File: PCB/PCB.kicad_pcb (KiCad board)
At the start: 2 copper layers, 150 x 150 mm, 14 parts

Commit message: resized and gerber
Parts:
- moved MotorFL1 58.0 mm to (99.1, 107.2), turned to 0 degrees
- moved MotorFR1 43.9 mm to (179.8, 106.6), turned to 180 degrees
- moved MotorBL1 34.5 mm to (99.1, 126.6), turned to 0 degrees
- moved MotorBR1 18.1 mm to (179.8, 126.0), turned to 180 degrees
- moved Battery1 14.7 mm to (154.8, 90.8)
- moved Buck_IN-1 9.28 mm to (163.3, 102.8)
- moved Buck_OUT-1 9.28 mm to (163.3, 122.8)
- moved Buck_IN+1 9.28 mm to (152.8, 102.8)
- moved Buck_OUT+1 9.28 mm to (152.8, 122.8)
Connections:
- PicoL1 pad 18: GND -> GND18
- PicoL1 pad 3: GND -> GND3
- PicoL1 pad 8: GND -> unconnected-(PicoL1-Pin_8-Pad8)
- PicoR1 pad 13: GND -> unconnected-(PicoR1-Pin_13-Pad13)
- PicoR1 pad 18: GND -> unconnected-(PicoR1-Pin_18-Pad18)
- PicoR1 pad 3: GND -> unconnected-(PicoR1-Pin_3-Pad3)
- PicoR1 pad 8: GND -> unconnected-(PicoR1-Pin_8-Pad8)
- QTR-8RC1 pad 11: GND -> GND3
- TB6612FNGL1 pad 1: GND -> unconnected-(TB6612FNGL1-Pin_1-Pad1)
- TB6612FNGR1 pad 3: GND -> GND18
- TB6612FNGR1 pad 8: GND -> unconnected-(TB6612FNGR1-Pin_8-Pad8)
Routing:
- net GND: track 451.5 -> 188.4 mm
- net Net-(MotorBL1-Pin_2): track 132.2 -> 45.3 mm
- net Net-(MotorBL1-Pin_1): track 138.7 -> 54.5 mm
- net Net-(MotorBR1-Pin_2): track 141.0 -> 69.4 mm
- net Net-(MotorBR1-Pin_1): track 143.3 -> 78.9 mm
- net GND18: track 0.00 -> 47.8 mm
- net GND3: track 0.00 -> 28.3 mm
- net VCC: track 77.0 -> 58.6 mm
- net /BuckOut: track 70.2 -> 63.4 mm
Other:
- board size 150 x 150 mm -> 100 x 115.5 mm

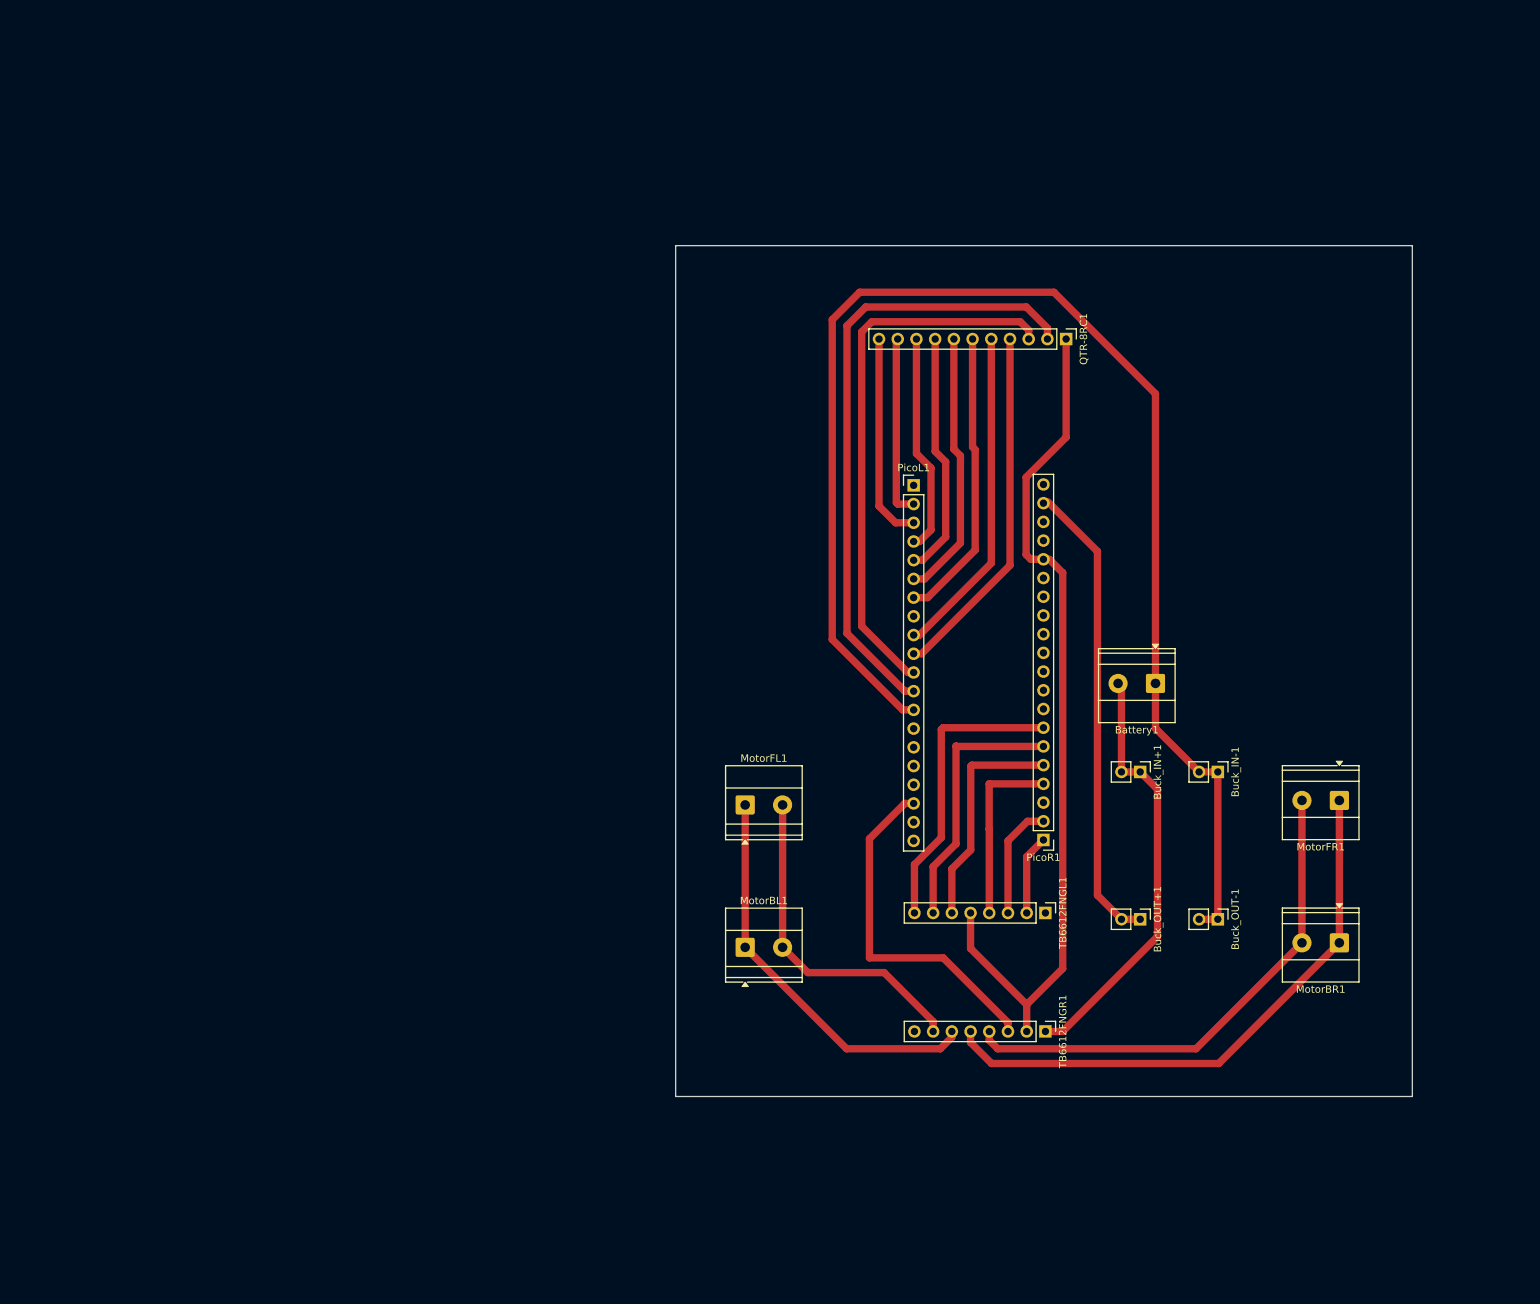
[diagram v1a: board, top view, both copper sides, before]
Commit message: page setup and pdf generation
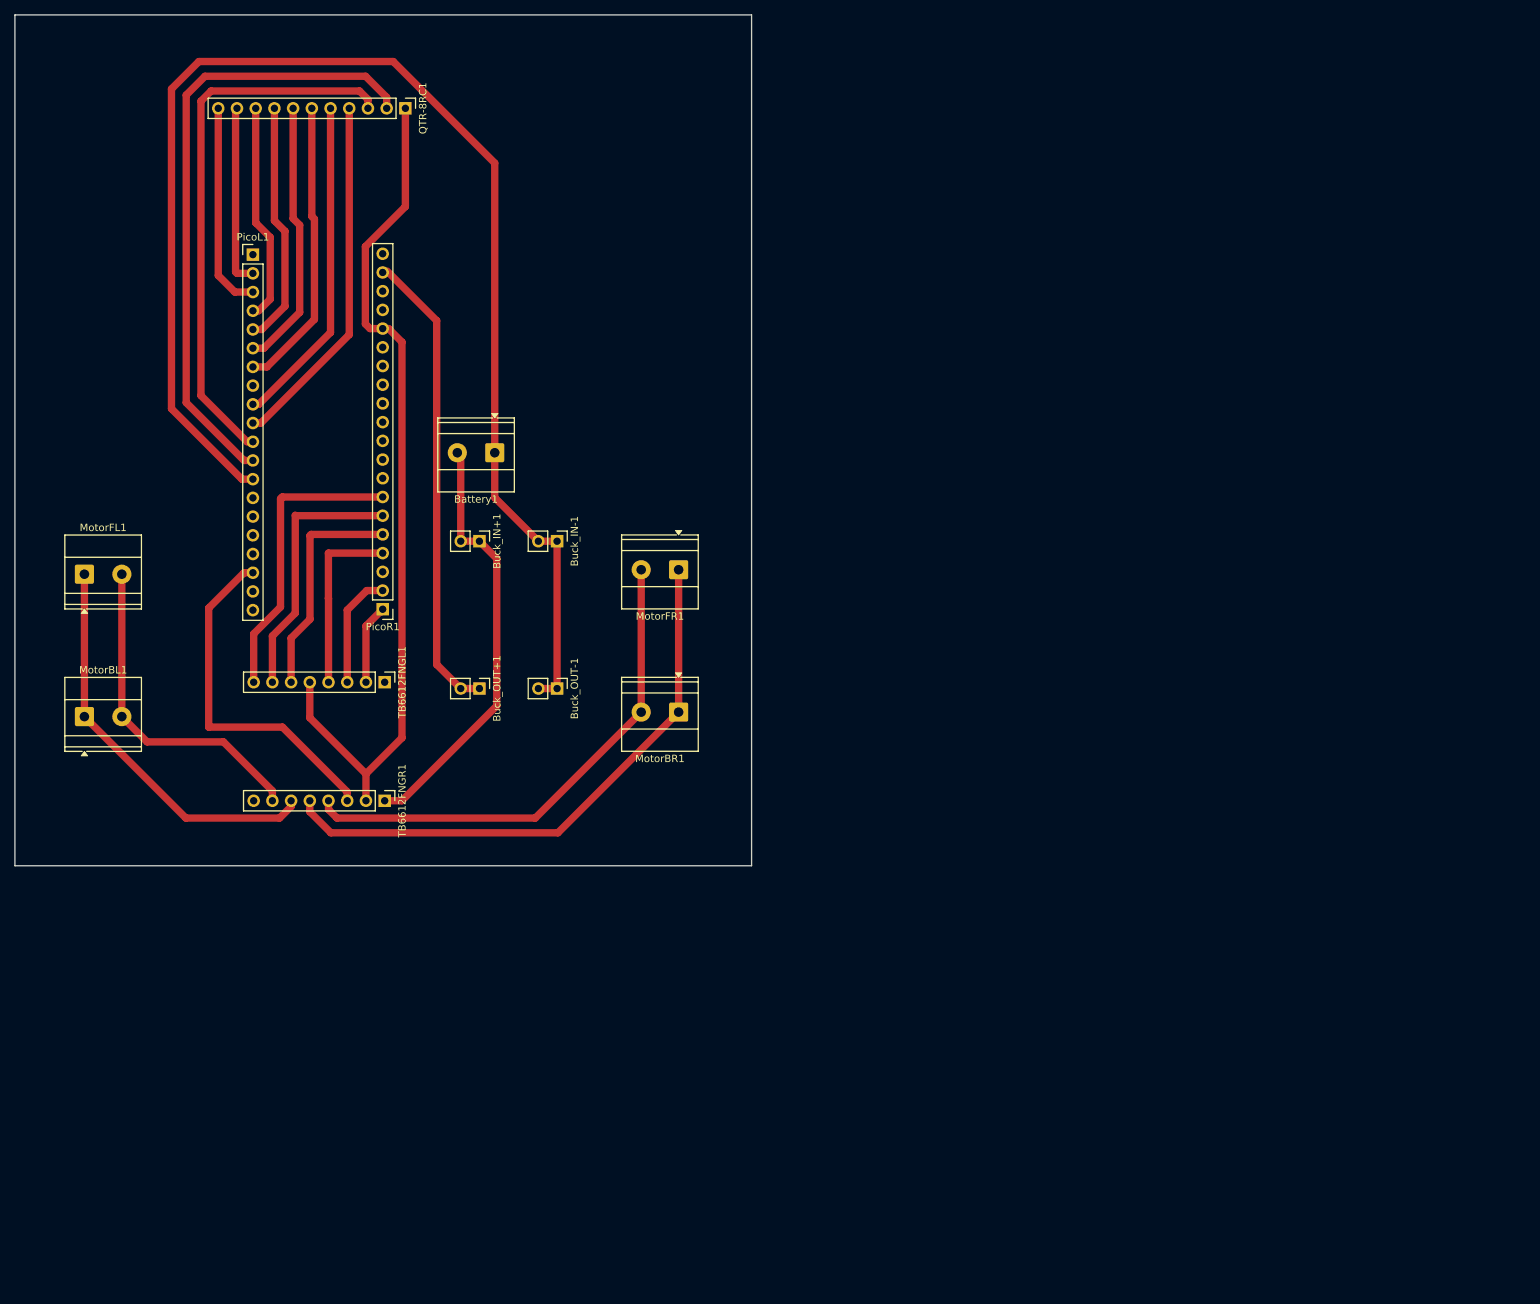
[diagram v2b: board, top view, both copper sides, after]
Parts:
- moved Battery1 95.0 mm to (65.1, 59.4)
- moved PicoR1 95.0 mm to (49.9, 80.7)
- moved Buck_IN+1 95.0 mm to (63.1, 71.4)
- moved Buck_IN-1 95.0 mm to (73.6, 71.4)
- moved Buck_OUT+1 95.0 mm to (63.1, 91.4)
- moved Buck_OUT-1 95.0 mm to (73.6, 91.4)
- moved MotorBL1 95.0 mm to (9.44, 95.3)
- moved MotorBR1 95.0 mm to (90.1, 94.6)
- moved MotorFL1 95.0 mm to (9.44, 75.9)
- moved MotorFR1 95.0 mm to (90.1, 75.3)
- moved PicoL1 95.0 mm to (32.3, 32.5)
- moved QTR-8RC1 95.0 mm to (53.0, 12.7)
- moved TB6612FNGL1 95.0 mm to (50.2, 90.6)
- moved TB6612FNGR1 95.0 mm to (50.2, 106.7)

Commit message: centralized
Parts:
- moved TB6612FNGL1 14.0 mm to (49.9, 104.5)
- moved Battery1 14.0 mm to (64.8, 73.4)
- moved PicoL1 14.0 mm to (32.0, 46.5)
- moved QTR-8RC1 14.0 mm to (52.7, 26.6)
- moved Buck_IN+1 14.0 mm to (62.7, 85.4)
- moved Buck_IN-1 14.0 mm to (73.3, 85.4)
- moved Buck_OUT+1 14.0 mm to (62.7, 105.4)
- moved Buck_OUT-1 14.0 mm to (73.3, 105.4)
- moved MotorBL1 14.0 mm to (9.13, 109.2)
- moved MotorBR1 14.0 mm to (89.8, 108.6)
- moved MotorFL1 14.0 mm to (9.13, 89.9)
- moved MotorFR1 14.0 mm to (89.8, 89.3)
- moved PicoR1 14.0 mm to (49.6, 94.6)
- moved TB6612FNGR1 14.0 mm to (49.9, 120.6)
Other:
- board size 100 x 115.5 mm -> 100 x 120 mm

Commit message: auto
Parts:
- moved TB6612FNGR1 110.9 mm to (22.3, 13.2), turned to 0 degrees
- moved TB6612FNGL1 101.3 mm to (6.16, 13.2), turned to 0 degrees
- moved MotorFR1 80.9 mm to (58.6, 14.7)
- moved MotorBR1 80.9 mm to (58.6, 34.0)
- moved MotorBL1 48.0 mm to (12.0, 61.3)
- moved MotorFL1 48.0 mm to (12.0, 42.0)
- moved Battery1 47.5 mm to (70.2, 26.2)
- moved Buck_IN+1 39.4 mm to (55.3, 46.7)
- moved Buck_IN-1 39.4 mm to (65.9, 46.7)
- moved Buck_OUT+1 39.4 mm to (55.3, 66.7)
- moved Buck_OUT-1 39.4 mm to (65.9, 66.7)
- moved PicoR1 28.0 mm to (43.9, 67.2)
- moved PicoL1 28.0 mm to (26.3, 19.1)
- moved QTR-8RC1 22.1 mm to (48.9, 4.90)
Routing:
- net Net-(PicoR1-Pin_1): track 10.8 -> 95.6 mm, vias 0 -> 1
- net GND: track 188.4 -> 105.5 mm, vias 0 -> 1
- net Net-(PicoR1-Pin_2): track 15.7 -> 92.8 mm, vias 0 -> 1
- net Net-(PicoR1-Pin_4): track 24.9 -> 93.2 mm, vias 0 -> 2
- net Net-(PicoR1-Pin_5): track 30.9 -> 84.7 mm, vias 0 -> 1
- net /3V3_OUT: track 117.4 -> 68.4 mm, vias 0 -> 1
- net Net-(PicoR1-Pin_7): track 40.4 -> 86.3 mm, vias 0 -> 2
- net Net-(PicoR1-Pin_6): track 35.8 -> 81.4 mm, vias 0 -> 1
- net Net-(PicoL1-Pin_12): track 85.0 -> 50.5 mm
- net VCC: track 58.6 -> 92.9 mm, vias 0 -> 1
- net Net-(PicoL1-Pin_11): track 74.5 -> 46.9 mm
- net Net-(MotorBR1-Pin_1): track 78.9 -> 61.0 mm
- net Net-(MotorBL1-Pin_1): track 54.5 -> 39.7 mm
- net Net-(MotorBR1-Pin_2): track 69.4 -> 82.8 mm, vias 0 -> 2
- net /BuckOut: track 63.4 -> 51.4 mm
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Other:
- board size 100 x 120 mm -> 75 x 75 mm

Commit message: 100x100
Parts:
- MotorBL1, MotorBR1, MotorFL1, MotorFR1: moved to B.Cu
- moved TB6612FNGR1 88.3 mm to (57.7, 94.1), turned to -90 degrees
- moved TB6612FNGL1 82.8 mm to (57.7, 78.0), turned to -90 degrees
- moved MotorFR1 82.3 mm to (89.0, 91.1)
- moved MotorFL1 50.0 mm to (21.8, 91.0)
- moved MotorBR1 48.5 mm to (89.0, 71.8)
- moved Buck_IN+1 15.6 mm to (67.0, 36.4)
- moved Buck_OUT+1 15.6 mm to (67.0, 56.4)
- moved Buck_IN-1 15.6 mm to (77.5, 36.4)
- moved Buck_OUT-1 15.6 mm to (77.5, 56.4)
- moved MotorBL1 14.3 mm to (21.8, 71.7)
- moved PicoL1 12.8 mm to (39.1, 19.1)
- moved PicoR1 12.8 mm to (56.7, 67.2)
- moved QTR-8RC1 11.6 mm to (60.5, 5.40)
- moved Battery1 8.70 mm to (74.6, 18.7)
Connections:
- PicoL1 pad 13: GND -> unconnected-(PicoL1-Pin_13-Pad13)
- PicoR1 pad 18: unconnected-(PicoR1-Pin_18-Pad18) -> GND
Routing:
- net Net-(PicoR1-Pin_1): track 95.6 -> 11.5 mm, vias 1 -> 0
- net Net-(PicoR1-Pin_2): track 92.8 -> 15.2 mm, vias 1 -> 0
- net Net-(PicoR1-Pin_4): track 93.2 -> 21.2 mm, vias 2 -> 0
- net Net-(PicoR1-Pin_5): track 84.7 -> 25.8 mm, vias 1 -> 0
- net Net-(PicoR1-Pin_7): track 86.3 -> 33.0 mm, vias 2 -> 0
- net Net-(PicoR1-Pin_6): track 81.4 -> 29.4 mm, vias 1 -> 0
- net /3V3_OUT: track 68.4 -> 105.3 mm, vias 1 -> 0
- net GND: track 105.5 -> 70.4 mm, vias 1 -> 0
- net Net-(MotorBR1-Pin_2): track 82.8 -> 55.8 mm, vias 2 -> 0
- net /BuckOut: track 51.4 -> 40.6 mm
- net VCC: track 92.9 -> 84.2 mm, vias 1 -> 0
- net GND18: track 45.7 -> 38.8 mm
- net Net-(MotorBL1-Pin_1): track 39.7 -> 46.0 mm
- net Net-(MotorBR1-Pin_1): track 61.0 -> 64.2 mm
- net Net-(MotorBL1-Pin_2): track 35.0 -> 37.5 mm
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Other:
- board size 75 x 75 mm -> 100 x 100 mm
- board text added: "MADE BY : HUZAIFA BAGHOOR"

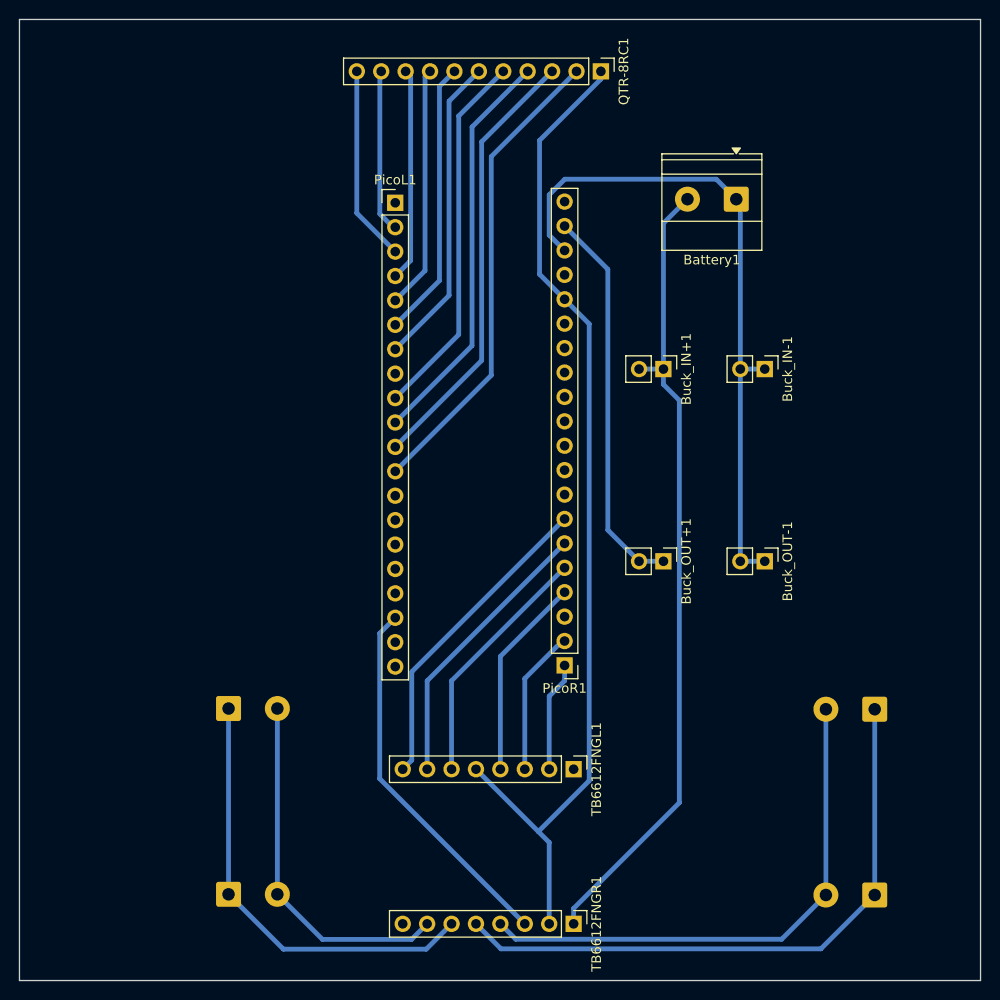
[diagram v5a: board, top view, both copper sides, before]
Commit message: 75x75 and names
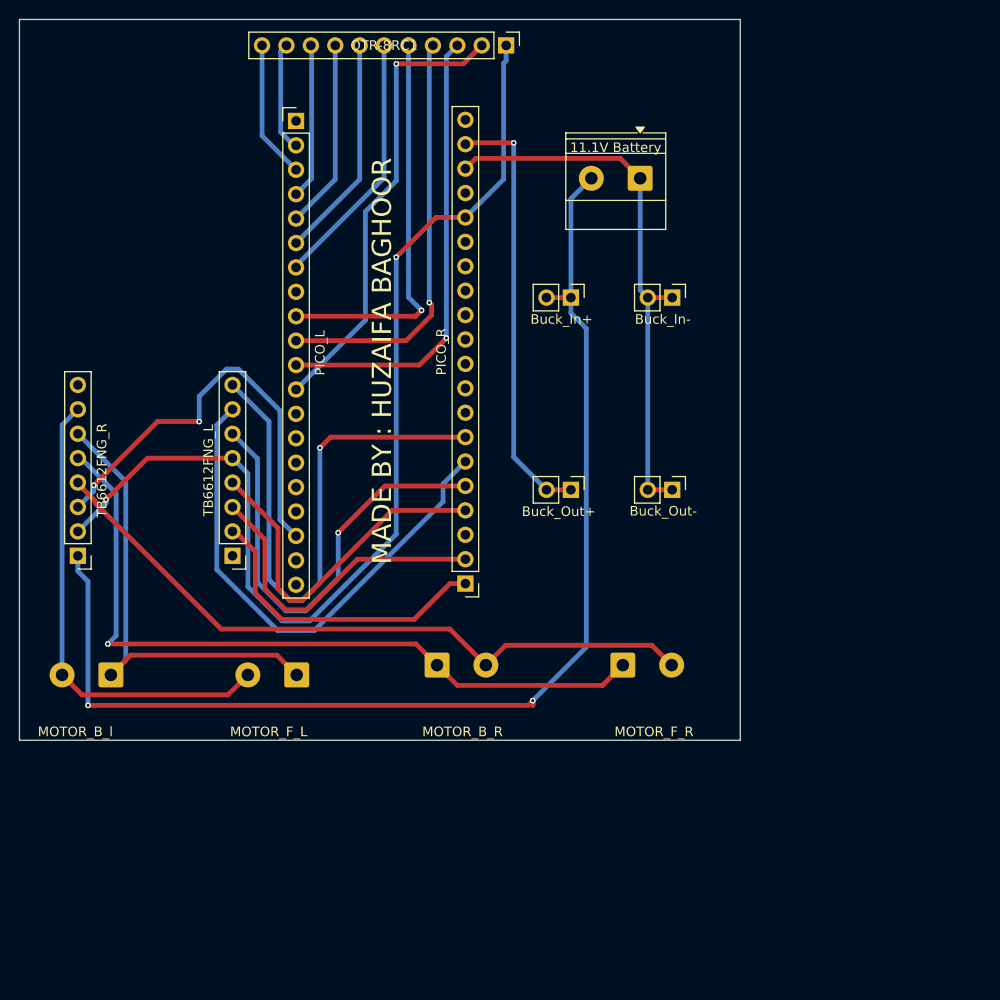
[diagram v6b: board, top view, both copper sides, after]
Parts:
- moved TB6612FNGR1 64.2 mm to (6.08, 55.8), turned to 180 degrees
- moved MotorBR1 45.8 mm to (43.5, 67.2), turned to 0 degrees
- moved TB6612FNGL1 41.9 mm to (22.2, 55.8), turned to 180 degrees
- moved MotorFR1 35.5 mm to (62.8, 67.2), turned to 0 degrees
- moved MotorFL1 23.9 mm to (28.8, 68.2), turned to 180 degrees
- moved PicoL1 13.4 mm to (28.8, 10.6)
- moved PicoR1 13.4 mm to (46.4, 58.7)
- moved MotorBL1 12.7 mm to (9.52, 68.2), turned to 180 degrees
- moved Buck_OUT+1 12.2 mm to (57.4, 48.9)
- moved Buck_IN+1 12.2 mm to (57.4, 28.9)
- moved Buck_OUT-1 12.2 mm to (67.9, 48.9)
- moved Buck_IN-1 12.2 mm to (67.9, 28.9)
- moved Battery1 10.2 mm to (64.6, 16.5)
- moved QTR-8RC1 10.2 mm to (50.6, 2.70)
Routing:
- net VCC: track 84.2 -> 125.2 mm, vias 0 -> 2
- net Net-(PicoR1-Pin_7): track 33.0 -> 58.4 mm, vias 0 -> 1
- net Net-(PicoR1-Pin_6): track 29.4 -> 54.2 mm
- net Net-(PicoR1-Pin_5): track 25.8 -> 47.6 mm, vias 0 -> 1
- net Net-(PicoR1-Pin_1): track 11.5 -> 32.1 mm
- net Net-(PicoR1-Pin_2): track 15.2 -> 33.9 mm
- net Net-(MotorBR1-Pin_2): track 55.8 -> 71.6 mm
- net Net-(PicoR1-Pin_4): track 21.2 -> 36.9 mm
- net Net-(MotorBR1-Pin_1): track 64.2 -> 77.8 mm, vias 0 -> 1
- net GND: track 70.4 -> 57.3 mm
- net Net-(MotorBL1-Pin_2): track 37.5 -> 49.4 mm
- net /3V3_OUT: track 105.3 -> 111.5 mm, vias 0 -> 2
- net GND3: track 20.4 -> 14.4 mm
- net Net-(PicoL1-Pin_4): track 22.2 -> 16.2 mm
- net Net-(PicoL1-Pin_2): track 17.1 -> 11.4 mm
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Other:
- board size 100 x 100 mm -> 75 x 75 mm
- board text added: "11.1V Battery"
- board text added: "Buck_In+"
- board text added: "Buck_In-"
- board text added: "Buck_Out+"
- board text added: "Buck_Out-"
- board text added: "MOTOR_B_R"
- board text added: "MOTOR_B_l"
- board text added: "MOTOR_F_L"
- board text added: "MOTOR_F_R"
- board text added: "PICO_L"
- board text added: "PICO_R"
- board text added: "QTR-8RC1"
- board text added: "TB6612FNG_L"
- board text added: "TB6612FNG_R"

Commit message: pdf
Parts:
- moved TB6612FNGR1 74.4 mm to (55.9, 111.1), turned to -90 degrees
- moved MotorBR1 56.6 mm to (90.0, 99.3), turned to 90 degrees
- moved TB6612FNGL1 51.7 mm to (55.9, 95.0), turned to -90 degrees
- moved MotorFR1 35.1 mm to (90.0, 45.0), turned to 90 degrees
- moved MotorFL1 33.6 mm to (11.5, 96.9), turned to 90 degrees
- moved Buck_OUT+1 32.0 mm to (71.0, 77.9)
- moved Buck_OUT-1 32.0 mm to (81.5, 77.9)
- moved Battery1 32.0 mm to (78.2, 45.4)
- moved Buck_IN+1 32.0 mm to (71.0, 57.9)
- moved Buck_IN-1 32.0 mm to (81.5, 57.9)
- moved PicoL1 26.2 mm to (38.2, 35.0)
- moved PicoR1 26.2 mm to (55.8, 83.1)
- moved MotorBL1 25.7 mm to (11.5, 42.6), turned to 90 degrees
- moved QTR-8RC1 24.1 mm to (59.7, 25.0)
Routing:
- net VCC: track 125.2 -> 0.00 mm, vias 2 -> 0
- net /3V3_OUT: track 111.5 -> 0.00 mm, vias 2 -> 0
- net Net-(MotorBR1-Pin_1): track 77.8 -> 0.00 mm, vias 1 -> 0
- net Net-(MotorBR1-Pin_2): track 71.6 -> 0.00 mm
- net Net-(PicoR1-Pin_7): track 58.4 -> 0.00 mm, vias 1 -> 0
- net GND: track 57.3 -> 0.00 mm
- net Net-(PicoR1-Pin_6): track 54.2 -> 0.00 mm
- net Net-(MotorBL1-Pin_2): track 49.4 -> 0.00 mm
- net Net-(MotorBL1-Pin_1): track 48.8 -> 0.00 mm
- net Net-(PicoL1-Pin_12): track 47.9 -> 0.00 mm, vias 1 -> 0
- net Net-(PicoL1-Pin_11): track 47.7 -> 0.00 mm, vias 1 -> 0
- net Net-(PicoR1-Pin_5): track 47.6 -> 0.00 mm, vias 1 -> 0
- net /BuckOut: track 45.1 -> 0.00 mm, vias 1 -> 0
- net GND18: track 44.4 -> 0.00 mm, vias 2 -> 0
- net Net-(PicoL1-Pin_10): track 43.5 -> 0.00 mm, vias 1 -> 0
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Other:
- board size 75 x 75 mm -> 100 x 100 mm
